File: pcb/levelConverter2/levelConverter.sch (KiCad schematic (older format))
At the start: 18 parts, among them Q1 BSS138, Q2 BSS138, Q3 BSS138, Q4 BSS138, Q5 BSS138, Q6 BSS138, Q7 BSS138, Q8 BSS138, U1 AP1117-33

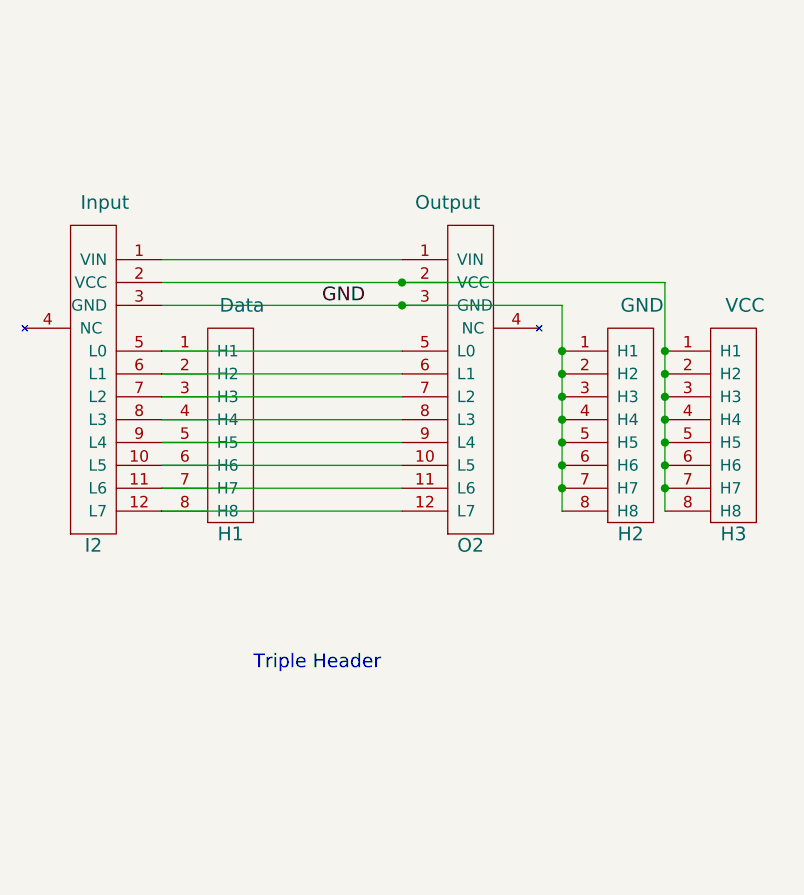
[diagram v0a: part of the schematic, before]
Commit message: Added terminal connectors to the header pins half module. Tweaked the MAX7219 module, and added both common anode and common cathode to stripLED modules.
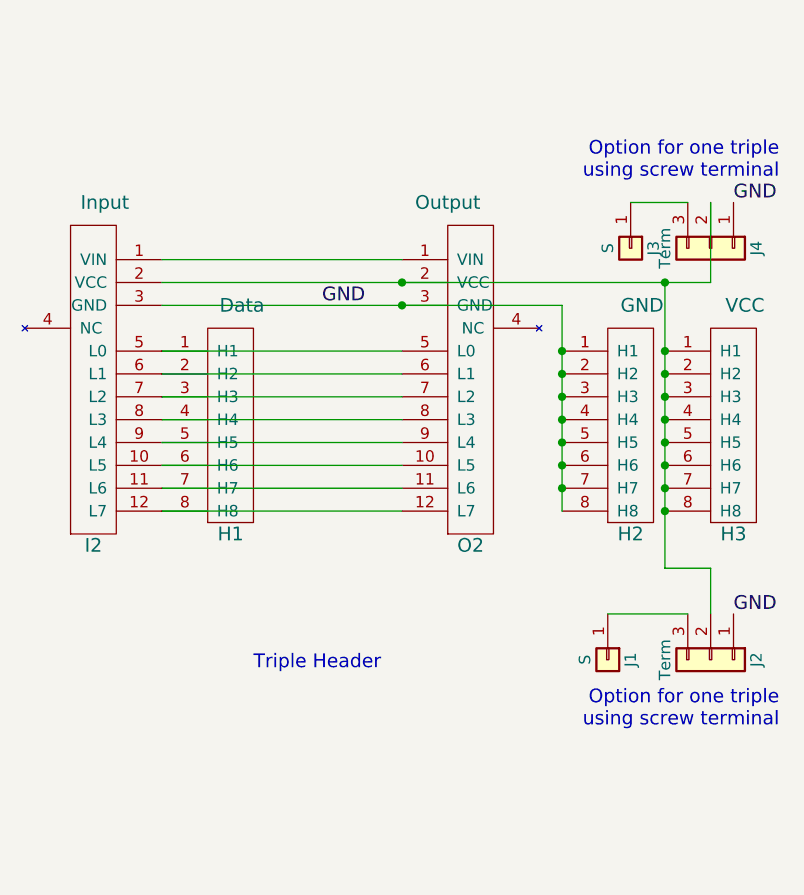
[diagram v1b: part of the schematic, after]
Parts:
- added J1, J3: S, Pin_Headers:Pin_Header_Straight_1x01_Pitch2.54mm, symbol Conn_01x01
- added J2, J4: Term, Connectors_Terminal_Blocks:TerminalBlock_Pheonix_MPT-2.54mm_3pol, symbol Conn_01x03
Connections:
- net Earth: now also J2.1 (Pin_1), J4.1 (Pin_1)
- net at H3.1 (H1), H3.2 (H2), H3.3 (H3)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: now also J2.2 (Pin_2), J4.2 (Pin_2)
- new net: J1.1 (Pin_1), J2.3 (Pin_3)
- new net: J3.1 (Pin_1), J4.3 (Pin_3)
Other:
- note added: "Option for one triple\nusing screw terminal"
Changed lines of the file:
@@
 	7250 1900 8300 1900
 Wire Wire Line
-	7250 2000 9450 2000
+	7250 2000 9650 2000
 Wire Wire Line
 	7250 2100 9000 2100
@@
 Connection ~ 9450 2400
 Wire Wire Line
-	9450 2000 9450 3000
+	9450 2000 9450 3250
 Text Label 7950 2100 0    60   ~ 0
 GND
@@
 Text Notes 7650 3700 0    60   ~ 0
 Triple Header
+$Comp
+L Conn_01x01 J1
+U 1 1 5AE81DFF
+P 9200 3650
+F 0 "J1" H 9200 3750 50  0000 C CNN
+F 1 "S" H 9200 3550 50  0000 C CNN
+F 2 "Pin_Headers:Pin_Header_Straight_1x01_Pitch2.54mm" H 9200 3650 50  0001 C CNN
+F 3 "" H 9200 3650 50  0001 C CNN
+	1    9200 3650
+	0    1    1    0
+$EndComp
+$Comp
+L Conn_01x03 J2
+U 1 1 5AE81E50
+P 9650 3650
+F 0 "J2" H 9650 3850 50  0000 C CNN
+F 1 "Term" H 9650 3450 50  0000 C CNN
+F 2 "Connectors_Terminal_Blocks:TerminalBlock_Pheonix_MPT-2.54mm_3pol" H 9650 3650 50  0001 C CNN
+F 3 "" H 9650 3650 50  0001 C CNN
+	1    9650 3650
+	0    1    1    0
+$EndComp
+Wire Wire Line
+	9200 3450 9550 3450
+Text Label 9750 3450 0    60   ~ 0
+GND
+$Comp
+L Conn_01x01 J3
+U 1 1 5AE82489
+P 9300 1850
+F 0 "J3" H 9300 1950 50  0000 C CNN
+F 1 "S" H 9300 1750 50  0000 C CNN
+F 2 "Pin_Headers:Pin_Header_Straight_1x01_Pitch2.54mm" H 9300 1850 50  0001 C CNN
+F 3 "" H 9300 1850 50  0001 C CNN
+	1    9300 1850
+	0    1    1    0
+$EndComp
+$Comp
+L Conn_01x03 J4
+U 1 1 5AE82510
+P 9650 1850
+F 0 "J4" H 9650 2050 50  0000 C CNN
+F 1 "Term" H 9650 1650 50  0000 C CNN
+F 2 "Connectors_Terminal_Blocks:TerminalBlock_Pheonix_MPT-2.54mm_3pol" H 9650 1850 50  0001 C CNN
+F 3 "" H 9650 1850 50  0001 C CNN
+	1    9650 1850
+	0    1    1    0
+$EndComp
+Text Label 9750 1650 0    60   ~ 0
+GND
+Wire Wire Line
+	9550 1650 9300 1650
+Wire Wire Line
+	9650 2000 9650 1650
+Connection ~ 9450 2000
+Wire Wire Line
+	9450 3250 9650 3250
+Wire Wire Line
+	9650 3250 9650 3450
+Connection ~ 9450 3000
+Text Notes 9950 3950 2    60   ~ 0
+Option for one triple\nusing screw terminal
+Text Notes 9950 1550 2    60   ~ 0
+Option for one triple\nusing screw terminal
 $EndSCHEMATC
